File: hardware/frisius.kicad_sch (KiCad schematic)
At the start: 0 parts

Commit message: fixing submodule
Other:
- added sheet User Interface (ui.kicad_sch)
- sheet BMS ports: added USB_POWER_GOOD; removed I_{bat}{+,-}, POWER_GOOD
- sheet Display B2B ports: added STATUS_LED_EXT; removed STATUS_LED, VDD_AUX_EN
- sheet Power ports: added none; removed I_{bat}{+,-}, PWR_CTRL{CORE_EN AUX_EN}, SENSOR_I2C{SDA SCL}
- sheet Processor ports: added SDMMC{D[0..3] CLK CMD}; removed PCTRL{CORE_EN AUX_EN}, SDMMC{D[0..3] CLK CMD CD}
- sheet SD Card ports: added SDMMC{D[0..3] CLK CMD}; removed SDMMC{D[0..3] CLK CMD CD}
- sheet USB ports: added USB_POWER_GOOD; removed USB_SW

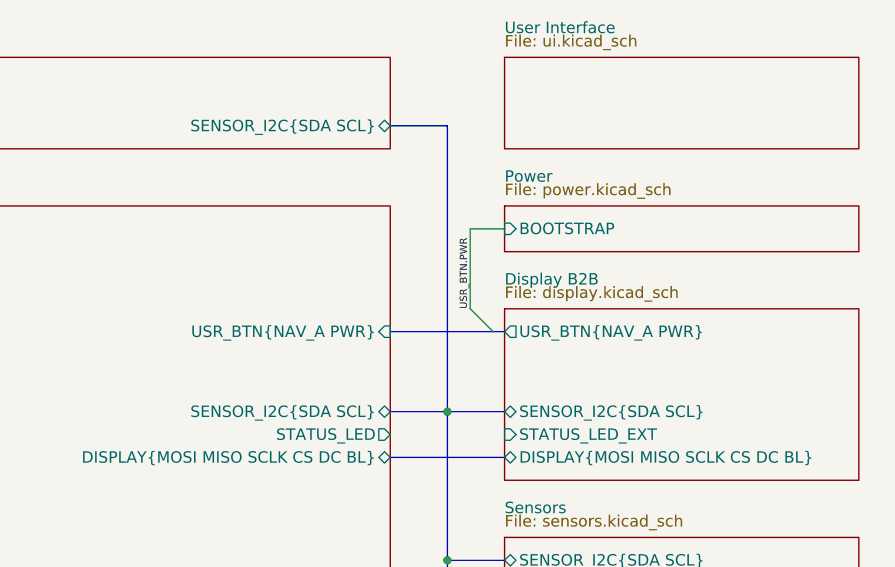
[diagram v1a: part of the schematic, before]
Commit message: schematic tidy up, component placement, shielding investigation
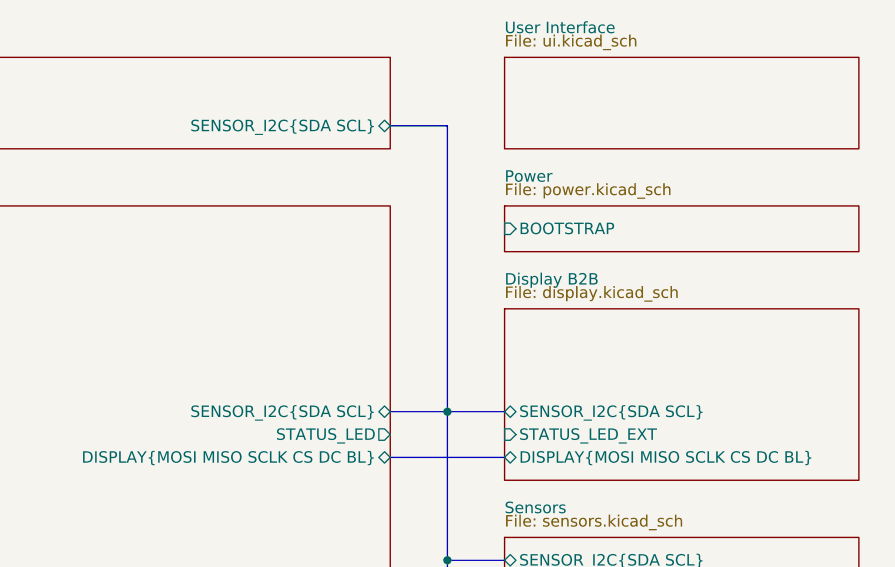
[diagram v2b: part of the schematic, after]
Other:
- sheet Display B2B ports: added none; removed USR_BTN{NAV_A PWR}
- sheet Processor ports: added none; removed USR_BTN{NAV_A PWR}

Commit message: Updates
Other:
- removed sheet BMS
- removed sheet USB
- removed sheet User Interface
- sheet Display B2B ports: added LCD_RGB{R[0..2] G[0..1] B[0..2]}, LCD_SPI{MOSI MISO SCLK CS DC BL}, NAV_BUTTON, POWER_BUTTON, STATUS_LED; removed DISPLAY{MOSI MISO SCLK CS DC BL}, STATUS_LED_EXT
- sheet Power: file power.kicad_sch -> usb.kicad_sch
- sheet Power ports: added BMS_INT, POWER_EN, SENSOR_I2C{SDA SCL}, USB_ESP{D+ D-; removed none
- sheet Processor ports: added BMS_INT, NAV_BUTTON, POWER_BUTTON, POWER_EN, USB_ESP{D+ D-; removed DEBUG_UART{RXD TXD}, DEV_BTN{BOOT RST}, USB_PRESENT

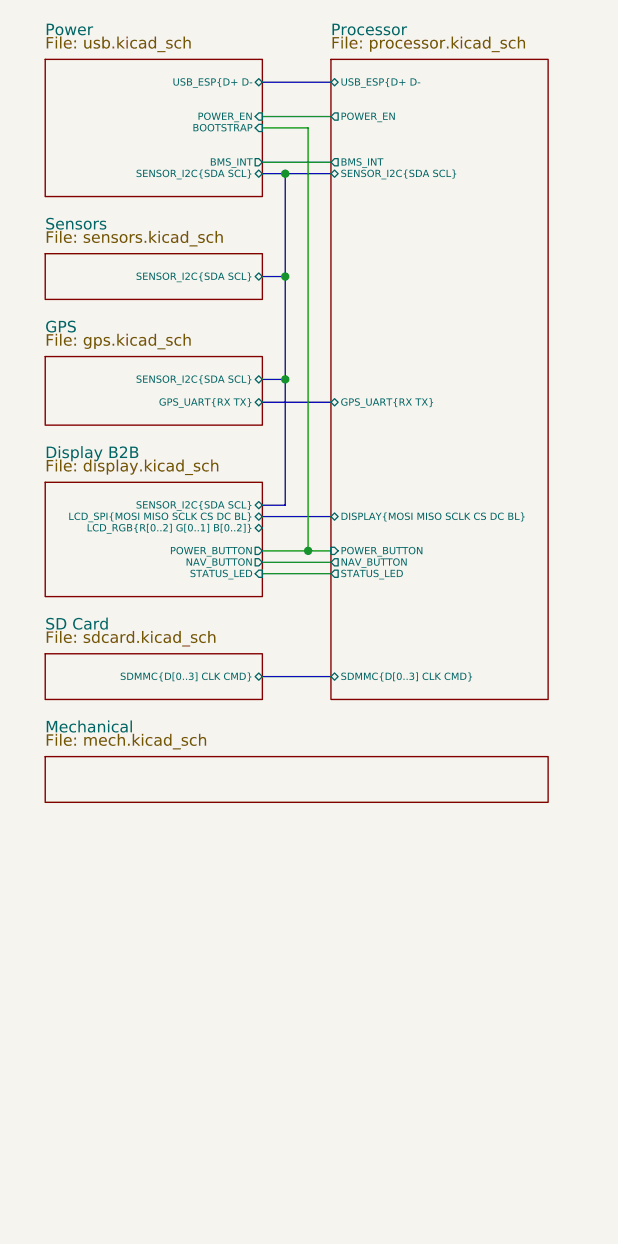
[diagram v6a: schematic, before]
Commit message: changing sdmmc to spi to support lcd rgb mode
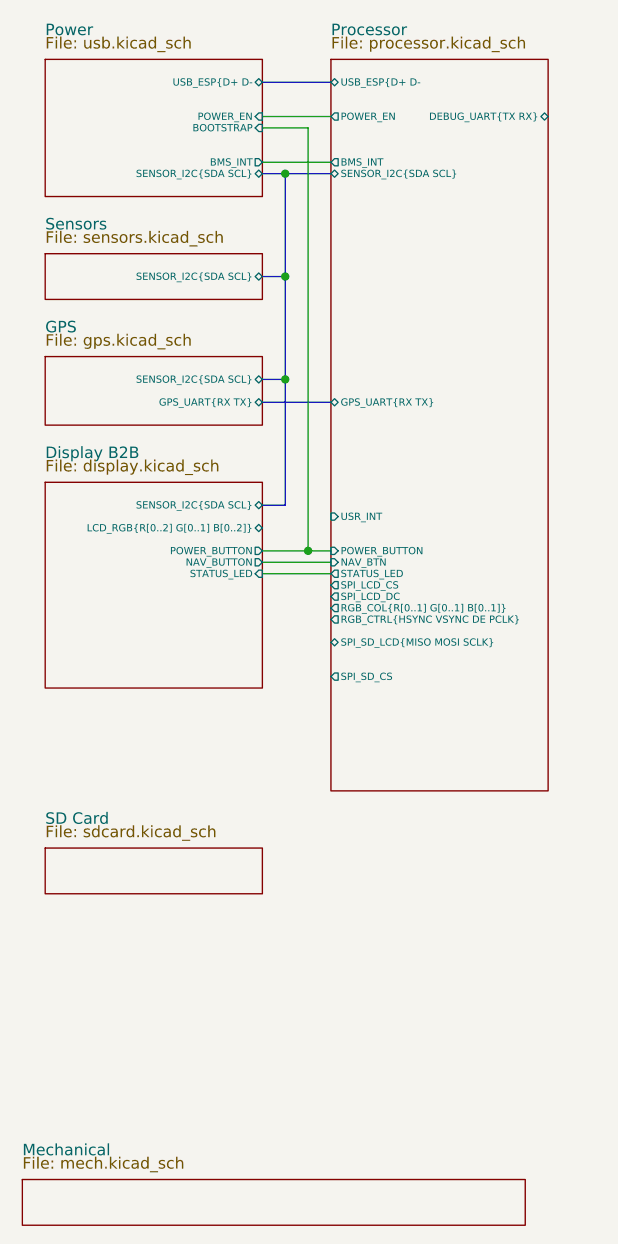
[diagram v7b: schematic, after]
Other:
- sheet Display B2B ports: added none; removed LCD_SPI{MOSI MISO SCLK CS DC BL}
- sheet Processor ports: added DEBUG_UART{TX RX}, NAV_BTN, RGB_COL{R[0..1] G[0..1] B[0..1]}, RGB_CTRL{HSYNC VSYNC DE PCLK}, SPI_LCD_CS, SPI_LCD_DC, SPI_SD_CS, SPI_SD_LCD{MISO MOSI SCLK}, USR_INT; removed DISPLAY{MOSI MISO SCLK CS DC BL}, NAV_BUTTON, SDMMC{D[0..3] CLK CMD}
- sheet SD Card ports: added none; removed SDMMC{D[0..3] CLK CMD}
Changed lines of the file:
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@@
   (junction (at 97.79 100.33) (diameter 0) (color 0 0 0 0)
   )
-  (bus (pts (xy 95.25 133.35) (xy 102.87 133.35))
-    (stroke (width 0) (type default) (color 0 0 0 0))
-  )
   (wire (pts (xy 100.33 119.38) (xy 100.33 72.39))
     (stroke (width 0) (type default) (color 0 0 0 0))
@@
     (stroke (width 0) (type default) (color 0 0 0 0))
   )
-  (bus (pts (xy 102.87 115.57) (xy 95.25 115.57))
-    (stroke (width 0) (type default) (color 0 0 0 0))
-  )
   (bus (pts (xy 102.87 102.87) (xy 95.25 102.87))
     (stroke (width 0) (type default) (color 0 0 0 0))
@@
     (stroke (width 0) (type default) (color 0 0 0 0))
   )
-  (sheet (at 71.12 130.81) (size 24.13 5.08)
-    (stroke (width 0.1524) (type solid) (color 0 0 0 0))
-    (fill (color 255 255 255 1.0000))
-    (property "Sheet name" "SD Card" (id 0) (at 71.12 128.27 0)
-      (effects (font (size 1.27 1.27)) (justify left bottom))
-    )
-    (property "Sheet file" "sdcard.kicad_sch" (id 1) (at 71.12 128.27 0)
-      (effects (font (size 1.27 1.27)) (justify left top))
-    )
-    (pin "SDMMC{D[0..3] CLK CMD}" bidirectional (at 95.25 133.35 0)
-      (effects (font (size 0.8 0.8)) (justify right))
-    )
-  )
-  (sheet (at 71.12 111.76) (size 24.13 12.7)
+  (sheet (at 71.12 152.4) (size 24.13 5.08)
+    (stroke (width 0.1524) (type solid) (color 0 0 0 0))
+    (fill (color 255 255 255 1.0000))
+    (property "Sheet name" "SD Card" (id 0) (at 71.12 149.86 0)
+      (effects (font (size 1.27 1.27)) (justify left bottom))
+    )
+    (property "Sheet file" "sdcard.kicad_sch" (id 1) (at 71.12 149.86 0)
+      (effects (font (size 1.27 1.27)) (justify left top))
+    )
+  )
+  (sheet (at 71.12 111.76) (size 24.13 22.86)
     (stroke (width 0.1524) (type solid) (color 0 0 0 0))
     (fill (color 255 255 255 1.0000))
@@
       (effects (font (size 0.8 0.8)) (justify right))
     )
-    (pin "LCD_SPI{MOSI MISO SCLK CS DC BL}" bidirectional (at 95.25 115.57 0)
-      (effects (font (size 0.8 0.8)) (justify right))
-    )
     (pin "LCD_RGB{R[0..2] G[0..1] B[0..2]}" bidirectional (at 95.25 116.84 0)
       (effects (font (size 0.8 0.8)) (justify right))
@@
     )
   )
-  (sheet (at 71.12 142.24) (size 55.88 5.08)
-    (stroke (width 0.1524) (type solid) (color 0 0 0 0))
-    (fill (color 255 255 255 1.0000))
-    (property "Sheet name" "Mechanical" (id 0) (at 71.12 139.7 0)
-      (effects (font (size 1.27 1.27)) (justify left bottom))
-    )
-    (property "Sheet file" "mech.kicad_sch" (id 1) (at 71.12 139.7 0)
+  (sheet (at 68.58 189.23) (size 55.88 5.08)
+    (stroke (width 0.1524) (type solid) (color 0 0 0 0))
+    (fill (color 255 255 255 1.0000))
+    (property "Sheet name" "Mechanical" (id 0) (at 68.58 186.69 0)
+      (effects (font (size 1.27 1.27)) (justify left bottom))
+    )
+    (property "Sheet file" "mech.kicad_sch" (id 1) (at 68.58 186.69 0)
       (effects (font (size 1.27 1.27)) (justify left top))
     )
@@
     )
   )
-  (sheet (at 102.87 64.77) (size 24.13 71.12)
+  (sheet (at 102.87 64.77) (size 24.13 81.28)
     (stroke (width 0.1524) (type solid) (color 0 0 0 0))
     (fill (color 255 255 255 1.0000))
@@
       (effects (font (size 1.27 1.27)) (justify left top))
     )
-    (pin "DISPLAY{MOSI MISO SCLK CS DC BL}" bidirectional (at 102.87 115.57 180)
-      (effects (font (size 0.8 0.8)) (justify left))
-    )
     (pin "GPS_UART{RX TX}" bidirectional (at 102.87 102.87 180)
       (effects (font (size 0.8 0.8)) (justify left))
@@
       (effects (font (size 0.8 0.8)) (justify left))
     )
-    (pin "NAV_BUTTON" output (at 102.87 120.65 180)
-      (effects (font (size 0.8 0.8)) (justify left))
-    )
     (pin "USB_ESP{D+ D-" bidirectional (at 102.87 67.31 180)
       (effects (font (size 0.8 0.8)) (justify left))
@@
       (effects (font (size 0.8 0.8)) (justify left))
     )
-    (pin "SDMMC{D[0..3] CLK CMD}" bidirectional (at 102.87 133.35 180)
-      (effects (font (size 0.8 0.8)) (justify left))
-    )
     (pin "POWER_BUTTON" input (at 102.87 119.38 180)
+      (effects (font (size 0.8 0.8)) (justify left))
+    )
+    (pin "SPI_LCD_CS" output (at 102.87 123.19 180)
+      (effects (font (size 0.8 0.8)) (justify left))
+    )
+    (pin "SPI_SD_CS" output (at 102.87 133.35 180)
+      (effects (font (size 0.8 0.8)) (justify left))
+    )
+    (pin "DEBUG_UART{TX RX}" bidirectional (at 127 71.12 0)
+      (effects (font (size 0.8 0.8)) (justify right))
+    )
+    (pin "SPI_SD_LCD{MISO MOSI SCLK}" bidirectional (at 102.87 129.54 180)
+      (effects (font (size 0.8 0.8)) (justify left))
+    )
+    (pin "NAV_BTN" input (at 102.87 120.65 180)
+      (effects (font (size 0.8 0.8)) (justify left))
+    )
+    (pin "SPI_LCD_DC" output (at 102.87 124.46 180)
+      (effects (font (size 0.8 0.8)) (justify left))
+    )
+    (pin "RGB_COL{R[0..1] G[0..1] B[0..1]}" output (at 102.87 125.73 180)
+      (effects (font (size 0.8 0.8)) (justify left))
+    )
+    (pin "USR_INT" input (at 102.87 115.57 180)
+      (effects (font (size 0.8 0.8)) (justify left))
+    )
+    (pin "RGB_CTRL{HSYNC VSYNC DE PCLK}" output (at 102.87 127 180)
       (effects (font (size 0.8 0.8)) (justify left))
     )
@@
       (reference "R59") (unit 1) (value "0") (footprint "Resistor_SMD:R_0402_1005Metric")
     )
-    (path "/de840488-ca73-469b-adda-a3c2d8f9c87a/01fbe2c1-1d29-4de1-9da1-a08b6ee3170e"
-      (reference "R?") (unit 1) (value "0") (footprint "")
-    )
     (path "/1c2dbee6-2600-45d3-a892-1b4f3056883c/09a6580e-3bde-4748-baa6-219e4cb1e45c"
       (reference "R?") (unit 1) (value "10k") (footprint "Resistor_SMD:R_0402_1005Metric")
@@
       (reference "R?") (unit 1) (value "22") (footprint "Resistor_SMD:R_0402_1005Metric")
     )
-    (path "/de840488-ca73-469b-adda-a3c2d8f9c87a/30eff275-8626-48d2-b426-066aedeb6e51"
-      (reference "R?") (unit 1) (value "0") (footprint "")
-    )
     (path "/d6a81b3b-912c-47c7-b234-5345a0da5522/31320b3f-3e55-45f7-a208-ce873488187e"
       (reference "R?") (unit 1) (value "0") (footprint "Resistor_SMD:R_0402_1005Metric")
@@
       (reference "R?") (unit 1) (value "1k") (footprint "Resistor_SMD:R_0402_1005Metric")
     )
-    (path "/de840488-ca73-469b-adda-a3c2d8f9c87a/7242959f-25af-4d5d-a827-7d85bab6eba7"
-      (reference "R?") (unit 1) (value "0") (footprint "")
-    )
     (path "/1c2dbee6-2600-45d3-a892-1b4f3056883c/84a1bb46-0da4-46f2-9b5c-8e1df418470f"
       (reference "R?") (unit 1) (value "10k") (footprint "Resistor_SMD:R_0402_1005Metric")
@@
       (reference "R?") (unit 1) (value "10k") (footprint "Resistor_SMD:R_0402_1005Metric")
     )
-    (path "/de840488-ca73-469b-adda-a3c2d8f9c87a/96b93f2f-7947-4652-9019-f99b9b7d988a"
-      (reference "R?") (unit 1) (value "0") (footprint "")
-    )
     (path "/d6a81b3b-912c-47c7-b234-5345a0da5522/afed0247-3087-4a0b-91ef-0185237acb71"
       (reference "R?") (unit 1) (value "100k") (footprint "Resistor_SMD:R_0402_1005Metric")
@@
       (reference "R?") (unit 1) (value "0") (footprint "Resistor_SMD:R_0402_1005Metric")
     )
+    (path "/d6a81b3b-912c-47c7-b234-5345a0da5522/ceabdb1d-70ea-427b-b4ad-7c22eaaaf4df"
+      (reference "R?") (unit 1) (value "0") (footprint "Resistor_SMD:R_0402_1005Metric")
+    )

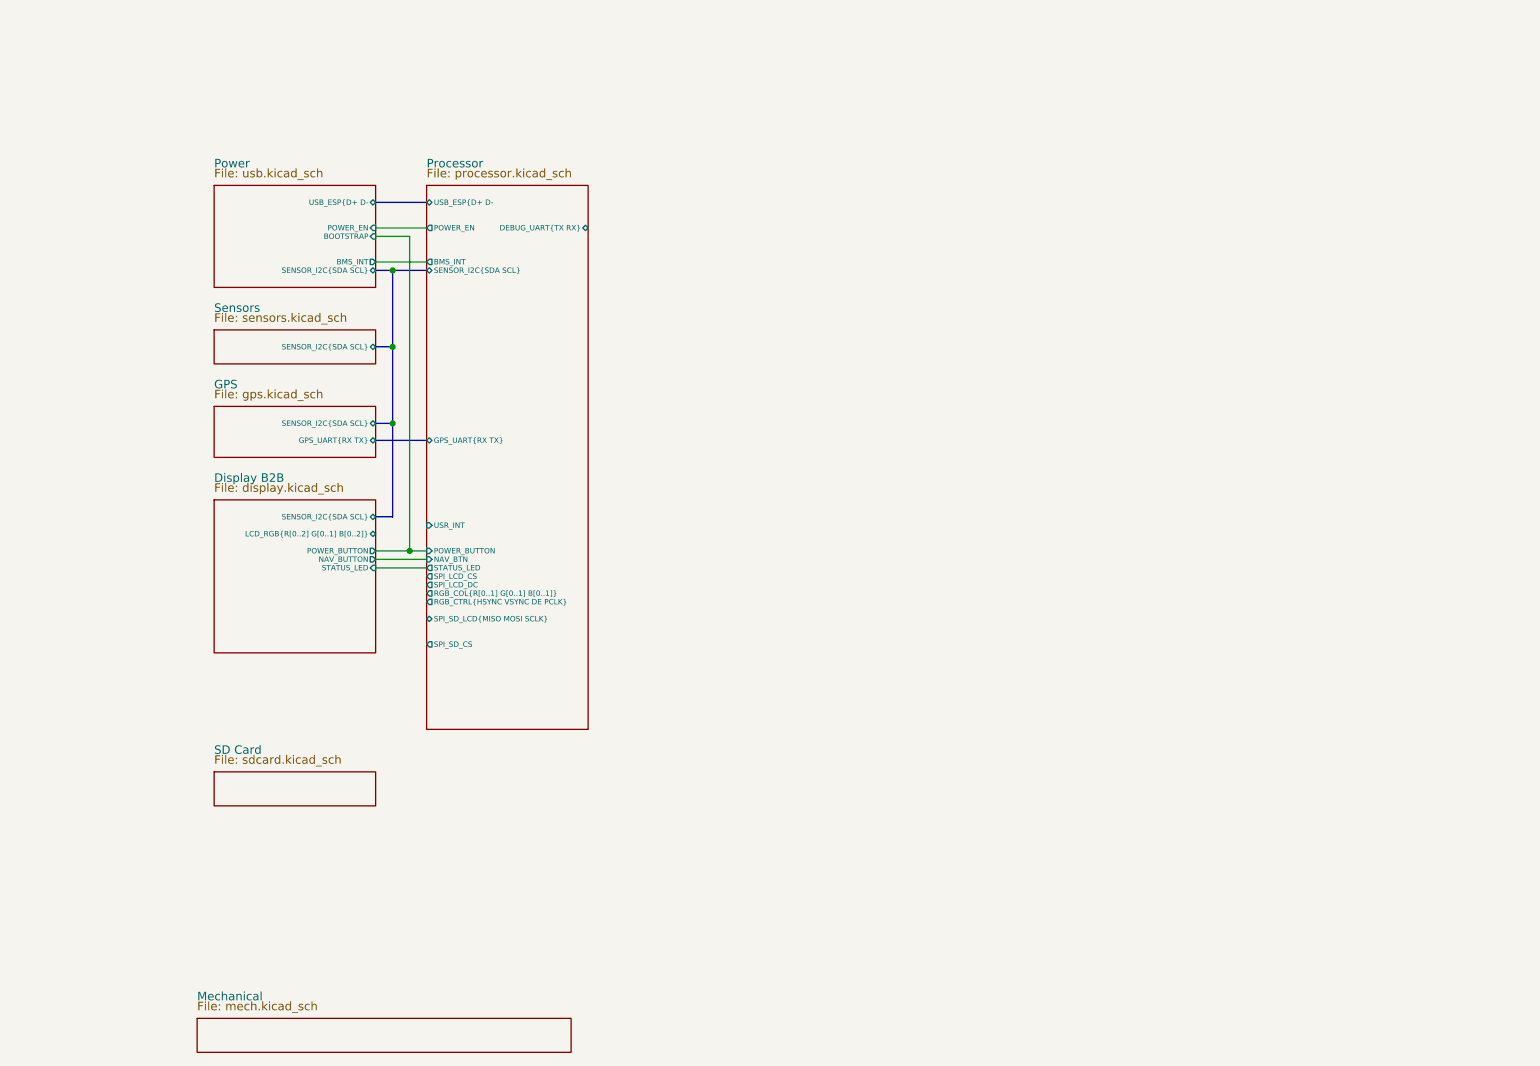
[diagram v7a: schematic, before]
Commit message: layout 0 unconnected
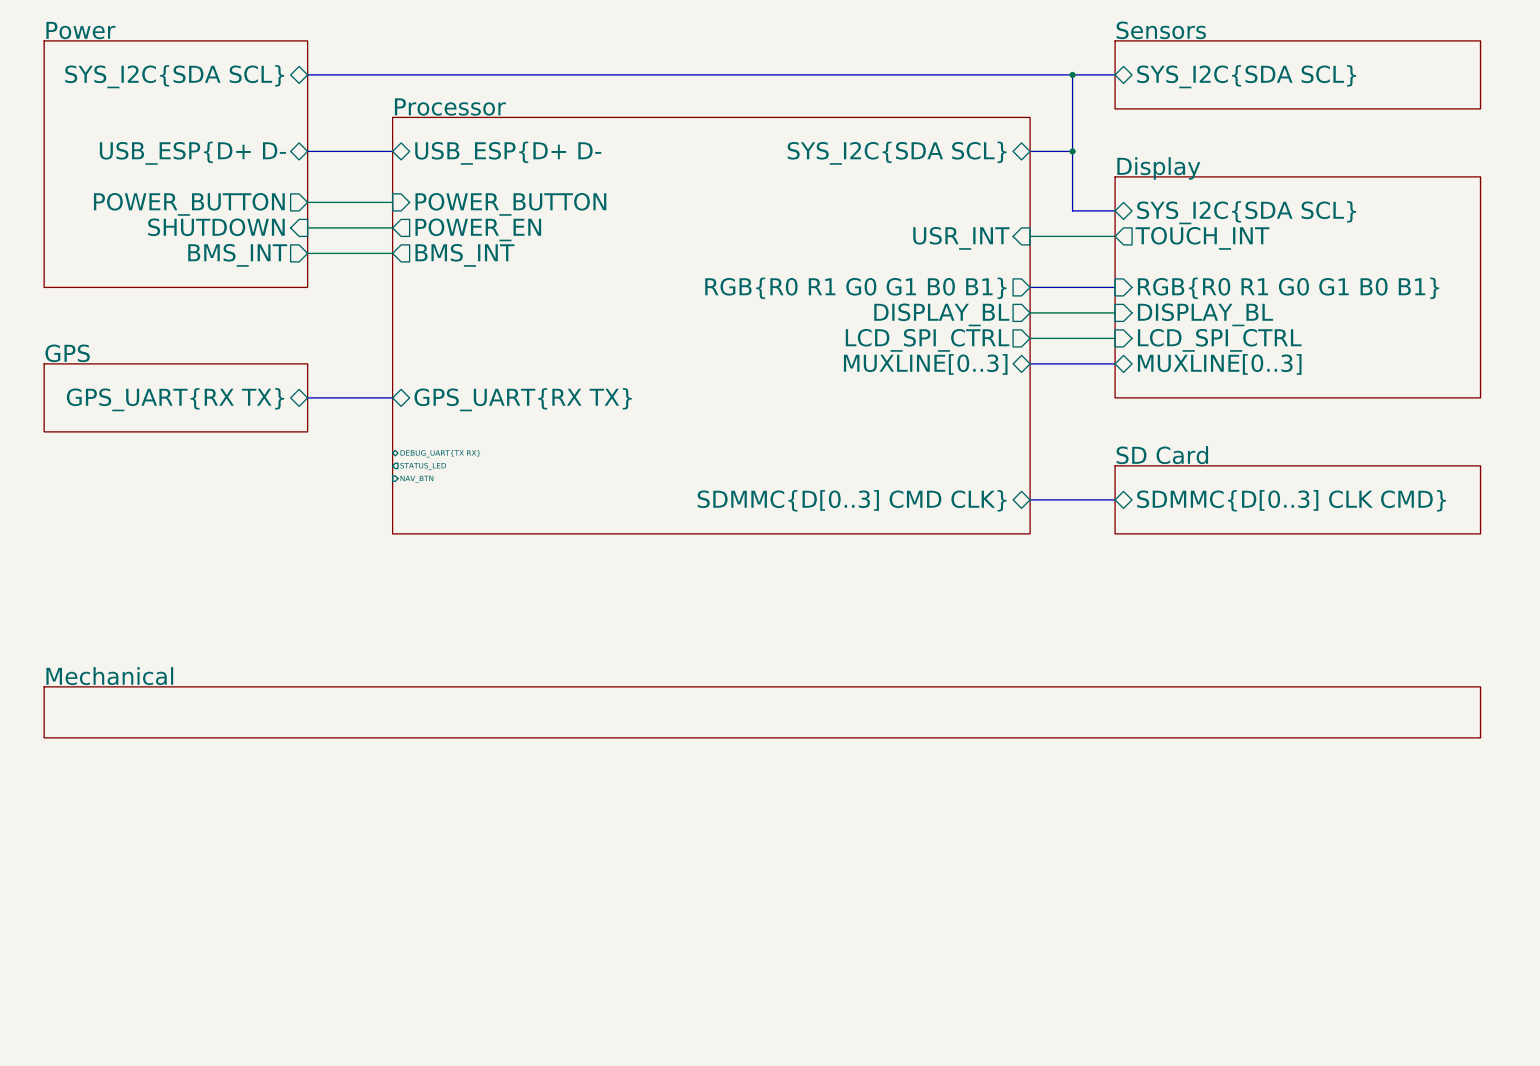
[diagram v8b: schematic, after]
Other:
- sheet Display B2B renamed Display
- sheet Display ports: added DISPLAY_BL, LCD_SPI_CTRL, MUXLINE[0..3], RGB{R0 R1 G0 G1 B0 B1}, SYS_I2C{SDA SCL}, TOUCH_INT; removed LCD_RGB{R[0..2] G[0..1] B[0..2]}, NAV_BUTTON, POWER_BUTTON, SENSOR_I2C{SDA SCL}, STATUS_LED
- sheet GPS ports: added none; removed SENSOR_I2C{SDA SCL}
- sheet Power ports: added POWER_BUTTON, SHUTDOWN, SYS_I2C{SDA SCL}; removed BOOTSTRAP, POWER_EN, SENSOR_I2C{SDA SCL}
- sheet Processor ports: added DISPLAY_BL, LCD_SPI_CTRL, MUXLINE[0..3], RGB{R0 R1 G0 G1 B0 B1}, SDMMC{D[0..3] CMD CLK}, SYS_I2C{SDA SCL}; removed RGB_COL{R[0..1] G[0..1] B[0..1]}, RGB_CTRL{HSYNC VSYNC DE PCLK}, SENSOR_I2C{SDA SCL}, SPI_LCD_CS, SPI_LCD_DC, SPI_SD_CS, SPI_SD_LCD{MISO MOSI SCLK}
- sheet SD Card ports: added SDMMC{D[0..3] CLK CMD}; removed none
- sheet Sensors ports: added SYS_I2C{SDA SCL}; removed SENSOR_I2C{SDA SCL}
